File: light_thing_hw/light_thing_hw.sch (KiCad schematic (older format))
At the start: 63 parts, among them J1 CONNECTORS, J2 Li-Ion Battery, J3 ADDR_LED_PANEL_1_CONNECTORS, J4 ADDR_LED_PANEL_2_CONNECTORS, J5 MIC_CONN, J6 3V3_TP, Q1 MMBF170, Q2 BSS83P, SW1 ST_USER_BUTTON1, SW2 ST_RESET_BUTTON, U1 BC832-V1, U3 MCP73833T-FCI_UN, U4 LMR62421XMF, U5 LP38511MRX-ADJ_NOPB, U6 STM32L476RGTx, U7 ICM-20600

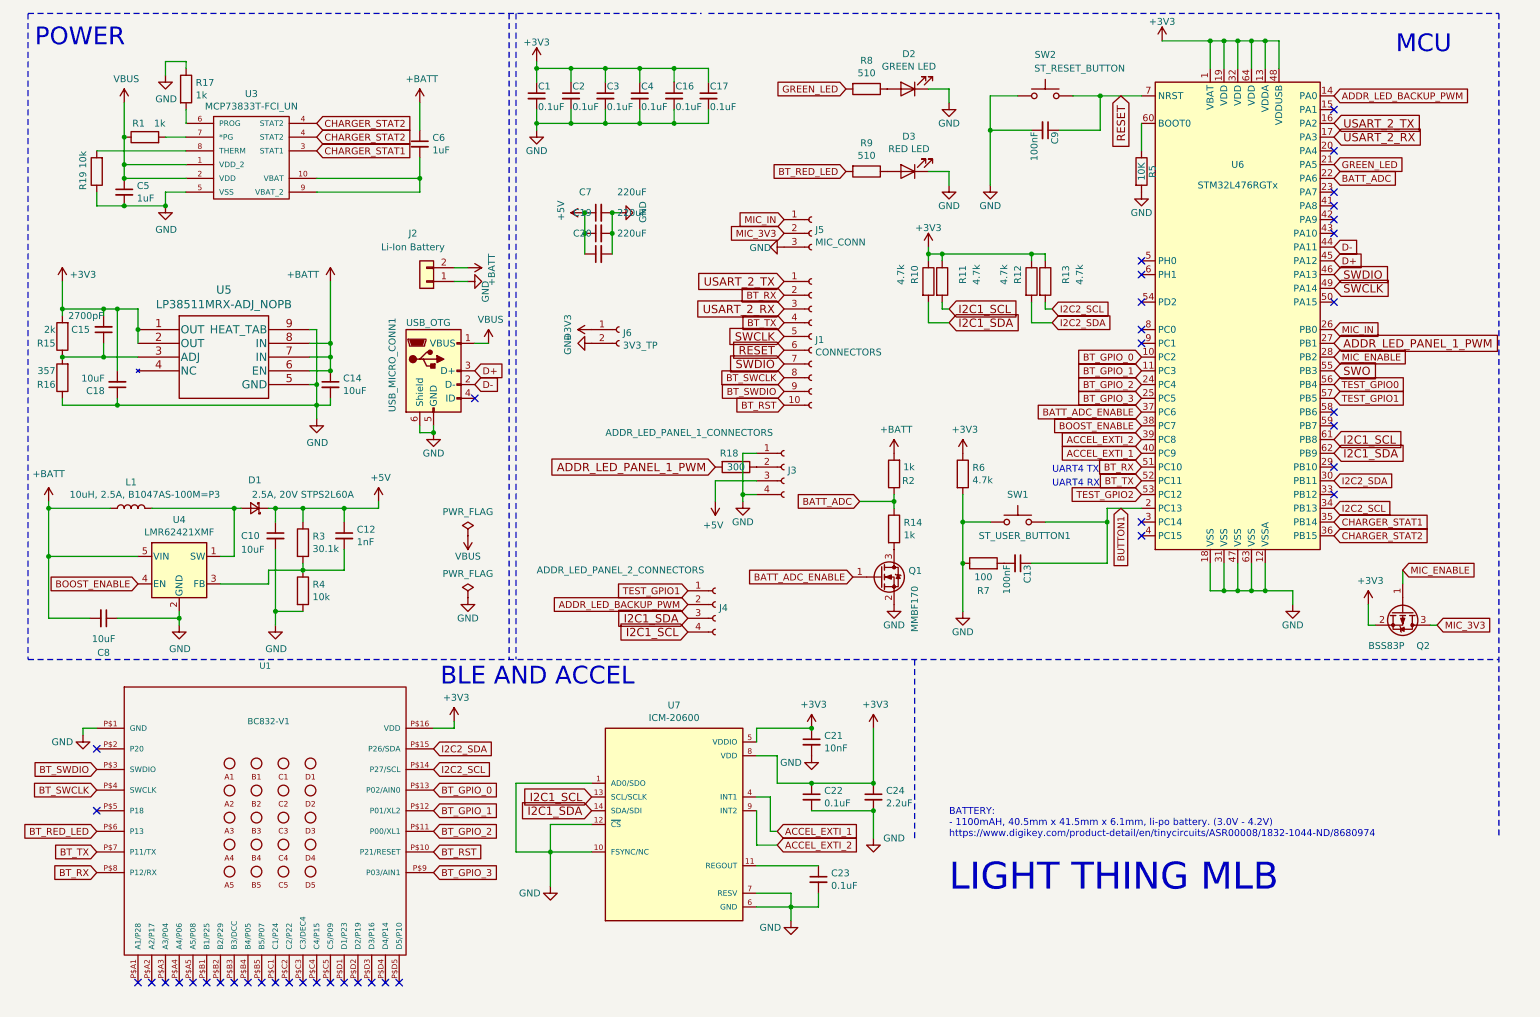
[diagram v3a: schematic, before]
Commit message: changed charger, reset button footprint
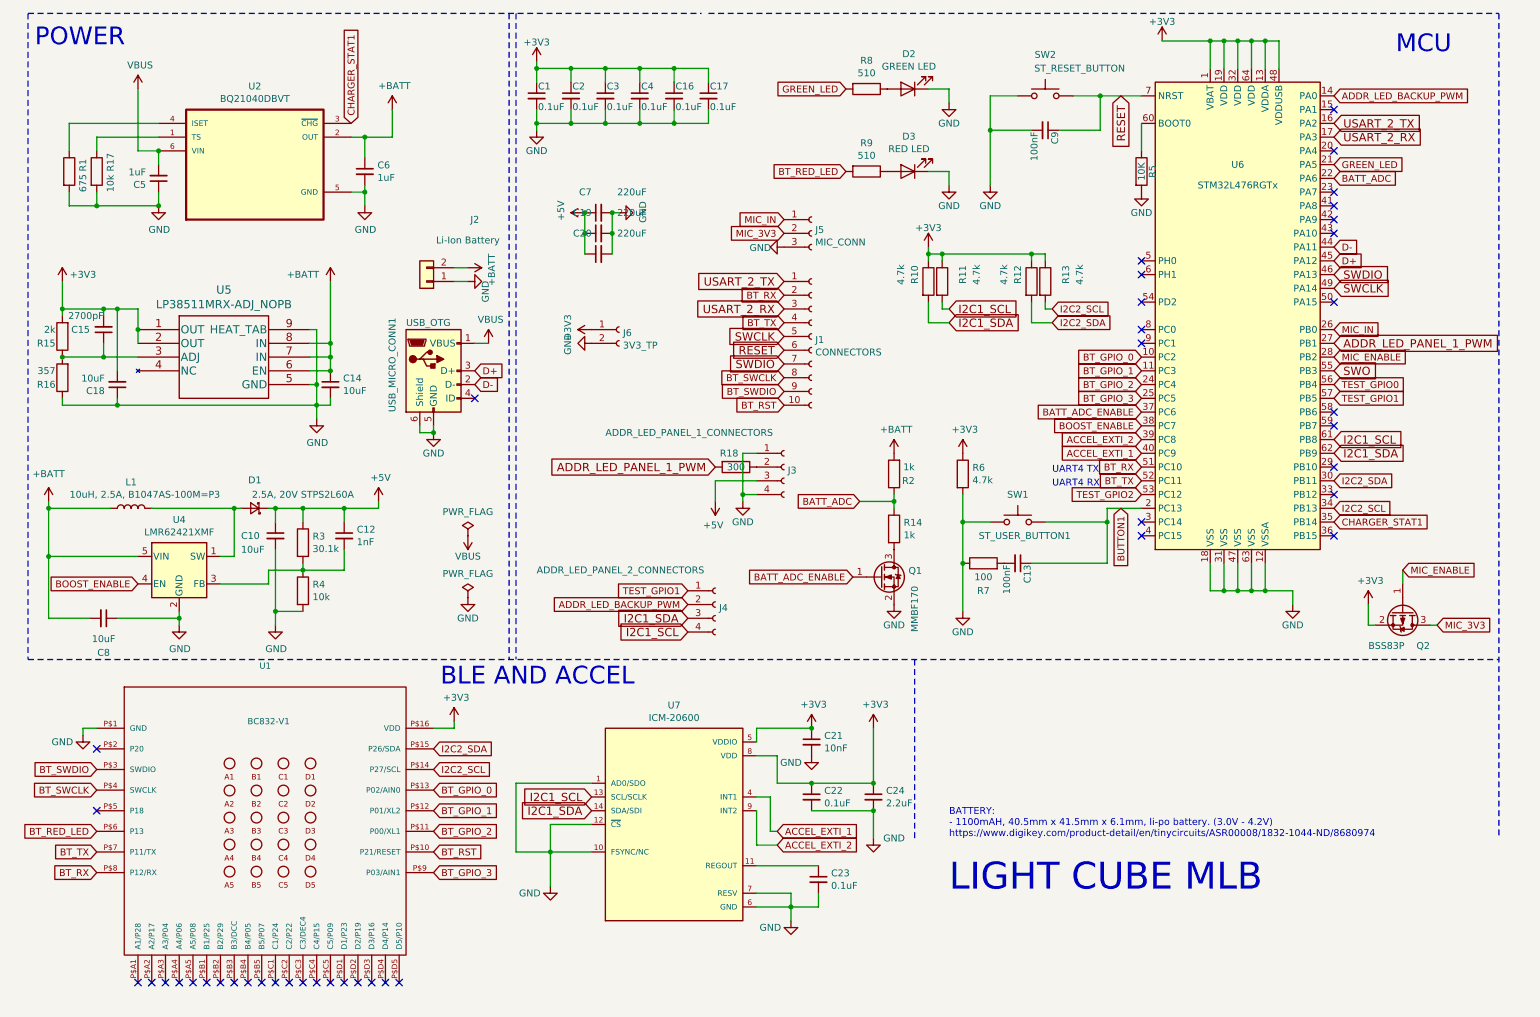
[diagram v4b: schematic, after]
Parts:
- removed R19: 10k, Resistor_SMD:R_0603_1608Metric_Pad1.05x0.95mm_HandSolder, symbol Device:R
- removed U3: MCP73833T-FCI_UN, footprints:MCP73833T-FCIUN-SMD, symbol MCP73833T-FCI_UN:MCP73833T-FCI_UN
- added U2: BQ21040DBVT, TI_BQ21040DBVT:SOT95P280X145-6N, symbol BQ21040DBVT:BQ21040DBVT
- R1: value 1k -> 675
- R17: value 1k -> 10k
- SW2: footprint Button_Switch_SMD:SW_SPST_PTS645 -> FSMSMTR_tactile_switch:SW_1437566-4
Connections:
- net +BATT: now also U2.2 (OUT)
- net CHARGER_STAT1: now also U2.3 (~CHG)
- net GND: now also C5.1, C6.2, R1.2, R17.2, U2.5 (GND); no longer C5.2, R17.1
- net VBUS: now also C5.2, U2.6 (VIN); no longer C5.1, R1.1
- net CHARGER_STAT2: no longer names the net of U6.36 (PB15)
- new net: R17.1, U2.1 (TS)
- new net: R1.1, U2.4 (ISET)
- no-connect marks 41 -> 42
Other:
- note added: "LIGHT CUBE MLB"
- note removed: "LIGHT THING MLB"
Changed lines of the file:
@@
 	11200 500  11200 6500
 Text Notes 7200 6900 0    196  ~ 0
-LIGHT THING MLB
+LIGHT CUBE MLB
 Connection ~ 8300 1100
 $Comp
@@
 U 1 1 5EC6ADFF
 P 3400 2450
-F 0 "J2" H 3500 2100 50  0000 C CNN
-F 1 "Li-Ion Battery" H 3500 2200 50  0000 C CNN
+F 0 "J2" H 3050 2000 50  0000 C CNN
+F 1 "Li-Ion Battery" H 3100 2150 50  0000 C CNN
 F 2 "Connector_JST:JST_SH_BM02B-SRSS-TB_1x02-1MP_P1.00mm_Vertical" H 3400 2450 50  0001 C CNN
 F 3 "~" H 3400 2450 50  0001 C CNN
@@
 F 0 "SW2" H 7900 1400 50  0000 C CNN
 F 1 "ST_RESET_BUTTON" H 8150 1300 50  0000 C CNN
-F 2 "Button_Switch_SMD:SW_SPST_PTS645" H 7900 1300 50  0001 C CNN
+F 2 "FSMSMTR_tactile_switch:SW_1437566-4" H 7900 1300 50  0001 C CNN
 F 3 "" H 7900 1300 50  0001 C CNN
 	1    7900 1100
@@
 BOOST_ENABLE
 $Comp
-L MCP73833T-FCI_UN:MCP73833T-FCI_UN U3
-U 1 1 5EF57FB2
-P 2450 1400
-F 0 "U3" H 2125 1715 50  0000 C CNN
-F 1 "MCP73833T-FCI_UN" H 2125 1624 50  0000 C CNN
-F 2 "footprints:MCP73833T-FCIUN-SMD" H 2500 1600 50  0001 L BNN
-F 3 "MSOP10" H 2900 1400 50  0001 L BNN
-F 4 "Microchip" H 2850 1500 50  0001 L BNN "Field4"
-F 5 "1605576" H 2900 1400 50  0001 L BNN "Field5"
-F 6 "88K5666" H 2900 1400 50  0001 L BNN "Field6"
-F 7 "MCP73833T-FCI/UN" H 2550 1700 50  0001 L BNN "Field7"
-	1    2450 1400
-	1    0    0    -1
-$EndComp
-$Comp
-L power:GND #PWR0104
-U 1 1 5EE8D240
-P 1500 1900
-F 0 "#PWR0104" H 1500 1650 50  0001 C CNN
-F 1 "GND" H 1505 1727 50  0000 C CNN
-F 2 "" H 1500 1900 50  0001 C CNN
-F 3 "" H 1500 1900 50  0001 C CNN
-	1    1500 1900
-	1    0    0    -1
-$EndComp
-Wire Wire Line
-	1500 1800 1500 1900
-Wire Wire Line
-	1650 1800 1500 1800
-$Comp
-L Device:R R1
-U 1 1 5EEA3D31
-P 1350 1400
-F 0 "R1" V 1450 1400 50  0000 L CNN
-F 1 "1k" V 1450 1250 50  0000 L CNN
-F 2 "Resistor_SMD:R_0603_1608Metric_Pad1.05x0.95mm_HandSolder" V 1280 1400 50  0001 C CNN
-F 3 "~" H 1350 1400 50  0001 C CNN
-F 4 "C21190" H 1350 1400 50  0001 C CNN "JLC_LIBRARY"
-	1    1350 1400
-	0    -1   -1   0
-$EndComp
-$Comp
-L Device:C_Small C5
-U 1 1 5EEAF533
-P 1200 1800
-F 0 "C5" H 1292 1846 50  0000 L CNN
-F 1 "1uF" H 1292 1755 50  0000 L CNN
-F 2 "Capacitor_SMD:C_0603_1608Metric_Pad1.05x0.95mm_HandSolder" H 1200 1800 50  0001 C CNN
-F 3 "~" H 1200 1800 50  0001 C CNN
-	1    1200 1800
-	1    0    0    -1
-$EndComp
-Wire Wire Line
-	1650 1700 1200 1700
-Wire Wire Line
-	1200 1700 1200 1600
-Wire Wire Line
-	1650 1600 1200 1600
-Connection ~ 1200 1600
-$Comp
 L power:VBUS #PWR0105
 U 1 1 5EEE9945
-P 1200 1150
-F 0 "#PWR0105" H 1200 1000 50  0001 C CNN
-F 1 "VBUS" H 1215 1323 50  0000 C CNN
-F 2 "" H 1200 1150 50  0001 C CNN
-F 3 "" H 1200 1150 50  0001 C CNN
-	1    1200 1150
-	1    0    0    -1
-$EndComp
-Connection ~ 1200 1700
-Wire Wire Line
-	1200 1900 1500 1900
-Connection ~ 1500 1900
-Wire Wire Line
-	1200 1150 1200 1400
-Connection ~ 1200 1400
-Wire Wire Line
-	1200 1400 1200 1600
-Wire Wire Line
-	1650 1400 1500 1400
-$Comp
-L Device:R R17
-U 1 1 5EF88860
-P 1650 1050
-F 0 "R17" H 1720 1096 50  0000 L CNN
-F 1 "1k" H 1720 1005 50  0000 L CNN
-F 2 "Resistor_SMD:R_0603_1608Metric_Pad1.05x0.95mm_HandSolder" V 1580 1050 50  0001 C CNN
-F 3 "~" H 1650 1050 50  0001 C CNN
-F 4 "C21190" H 1650 1050 50  0001 C CNN "JLC_LIBRARY"
-	1    1650 1050
-	1    0    0    -1
-$EndComp
-Wire Wire Line
-	3350 1800 3350 1700
-$Comp
-L Device:C_Small C6
-U 1 1 5EFBB5E4
-P 3350 1450
-F 0 "C6" H 3442 1496 50  0000 L CNN
-F 1 "1uF" H 3442 1405 50  0000 L CNN
-F 2 "Capacitor_SMD:C_0603_1608Metric_Pad1.05x0.95mm_HandSolder" H 3350 1450 50  0001 C CNN
-F 3 "~" H 3350 1450 50  0001 C CNN
-	1    3350 1450
-	1    0    0    -1
-$EndComp
-Wire Wire Line
-	3350 1700 3350 1550
-Connection ~ 3350 1700
-Wire Wire Line
-	3350 1350 3350 1150
+P 1300 1050
+F 0 "#PWR0105" H 1300 900 50  0001 C CNN
+F 1 "VBUS" H 1315 1223 50  0000 C CNN
+F 2 "" H 1300 1050 50  0001 C CNN
+F 3 "" H 1300 1050 50  0001 C CNN
+	1    1300 1050
+	1    0    0    -1
+$EndComp
+Wire Wire Line
+	3150 1400 3150 1200
 $Comp
 L power:+BATT #PWR0106
 U 1 1 5EFE21D4
-P 3350 1150
-F 0 "#PWR0106" H 3350 1000 50  0001 C CNN
-F 1 "+BATT" H 3365 1323 50  0000 C CNN
-F 2 "" H 3350 1150 50  0001 C CNN
-F 3 "" H 3350 1150 50  0001 C CNN
-	1    3350 1150
-	1    0    0    -1
-$EndComp
-$Comp
-L power:GND #PWR0107
-U 1 1 5F03E671
-P 1500 950
-F 0 "#PWR0107" H 1500 700 50  0001 C CNN
-F 1 "GND" H 1505 777 50  0000 C CNN
-F 2 "" H 1500 950 50  0001 C CNN
-F 3 "" H 1500 950 50  0001 C CNN
-	1    1500 950
-	1    0    0    -1
-$EndComp
-Wire Wire Line
-	1650 1200 1650 1300
-Wire Wire Line
-	1650 900  1650 850
-Wire Wire Line
-	1650 850  1500 850
-Wire Wire Line
-	1500 850  1500 950
+P 3150 1200
+F 0 "#PWR0106" H 3150 1050 50  0001 C CNN
+F 1 "+BATT" H 3165 1373 50  0000 C CNN
+F 2 "" H 3150 1200 50  0001 C CNN
+F 3 "" H 3150 1200 50  0001 C CNN
+	1    3150 1200
+	1    0    0    -1
+$EndComp
 Wire Wire Line
 	3750 2900 3850 2900
-Text GLabel 2600 1500 2    50   Input ~ 0
+Text GLabel 2850 1300 1    50   Input ~ 0
 CHARGER_STAT1
 Connection ~ 2700 3100
@@
 	3050 4100 2800 4100
 Connection ~ 2800 4100
-Wire Wire Line
-	2600 1800 3350 1800
-Wire Wire Line
-	2600 1700 3350 1700
 Text GLabel 5300 4800 0    50   Input ~ 0
 ADDR_LED_BACKUP_PWM
@@
 Text GLabel 10000 4200 2    50   Input ~ 0
 CHARGER_STAT1
-Text GLabel 10000 4300 2    50   Input ~ 0
-CHARGER_STAT2
 Text GLabel 10000 3000 2    50   Input ~ 0
 MIC_ENABLE
@@
 NoConn ~ 10000 3400
 NoConn ~ 10000 3500
-Wire Wire Line
-	1650 1500 1000 1500
-$Comp
-L Device:R R19
-U 1 1 6006B026
-P 1000 1650
-F 0 "R19" V 1100 1650 50  0000 L CNN
-F 1 "10k" V 1100 1500 50  0000 L CNN
-F 2 "Resistor_SMD:R_0603_1608Metric_Pad1.05x0.95mm_HandSolder" V 930 1650 50  0001 C CNN
-F 3 "~" H 1000 1650 50  0001 C CNN
-F 4 "C21190" H 1000 1650 50  0001 C CNN "JLC_LIBRARY"
-	1    1000 1650
-	-1   0    0    1
-$EndComp
-Wire Wire Line
-	1000 1800 1000 1900
-Wire Wire Line
-	1000 1900 1200 1900
-Connection ~ 1200 1900
 $Comp
 L power:GND #PWR0112
@@
 Text GLabel 5300 5000 0    60   Input ~ 0
 I2C1_SCL
-Text GLabel 2600 1400 2    50   Input ~ 0
-CHARGER_STAT2
-Text GLabel 2600 1300 2    50   Input ~ 0
-CHARGER_STAT2
 Text GLabel 6000 2100 0    50   Input ~ 0
 MIC_3V3
@@
 Wire Wire Line
 	4050 6600 4300 6600
+$Comp
+L BQ21040DBVT:BQ21040DBVT U2
+U 1 1 60135CA1
+P 2150 1600
+F 0 "U2" H 2150 2170 50  0000 C CNN
+F 1 "BQ21040DBVT" H 2150 2079 50  0000 C CNN
+F 2 "TI_BQ21040DBVT:SOT95P280X145-6N" H 2150 1600 50  0001 L BNN
+F 3 "" H 2150 1600 50  0001 L BNN
+	1    2150 1600
+	1    0    0    -1
+$EndComp
+Wire Wire Line
+	2850 1800 2950 1800
+Wire Wire Line
+	2950 1800 2950 1900
+$Comp
+L power:GND #PWR0104
+U 1 1 601452F4
+P 2950 1900
+F 0 "#PWR0104" H 2950 1650 50  0001 C CNN
+F 1 "GND" H 2955 1727 50  0000 C CNN
+F 2 "" H 2950 1900 50  0001 C CNN
+F 3 "" H 2950 1900 50  0001 C CNN
+	1    2950 1900
+	1    0    0    -1
+$EndComp
+Wire Wire Line
+	2950 1750 2950 1800
+Connection ~ 2950 1800
+Wire Wire Line
+	2950 1550 2950 1400
+Wire Wire Line
+	2950 1400 2850 1400
+Wire Wire Line
+	2950 1400 3150 1400
+Connection ~ 2950 1400
+$Comp
+L Device:R R17
+U 1 1 601ECAC0
+P 1000 1650
+F 0 "R17" V 1100 1650 50  0000 L CNN
+F 1 "10k" V 1100 1500 50  0000 L CNN
+F 2 "Resistor_SMD:R_0603_1608Metric_Pad1.05x0.95mm_HandSolder" V 930 1650 50  0001 C CNN
+F 3 "~" H 1000 1650 50  0001 C CNN
+F 4 "C21190" H 1000 1650 50  0001 C CNN "JLC_LIBRARY"
+	1    1000 1650
+	1    0    0    -1
+$EndComp
+$Comp
+L power:GND #PWR0107
+U 1 1 602388CD
+P 1450 1900
+F 0 "#PWR0107" H 1450 1650 50  0001 C CNN
+F 1 "GND" H 1455 1727 50  0000 C CNN
+F 2 "" H 1450 1900 50  0001 C CNN
+F 3 "" H 1450 1900 50  0001 C CNN
+	1    1450 1900
+	1    0    0    -1
+$EndComp
+Wire Wire Line
+	1000 1500 1000 1400
+Wire Wire Line
+	1000 1400 1450 1400
+Wire Wire Line
+	1000 1800 1000 1900
+Wire Wire Line
+	1000 1900 1450 1900
+$Comp
+L Device:R R1
+U 1 1 602AD118
+P 800 1650
+F 0 "R1" V 900 1650 50  0000 L CNN
+F 1 "675" V 900 1500 50  0000 L CNN
+F 2 "Resistor_SMD:R_0603_1608Metric_Pad1.05x0.95mm_HandSolder" V 730 1650 50  0001 C CNN
+F 3 "~" H 800 1650 50  0001 C CNN
+F 4 "C21190" H 800 1650 50  0001 C CNN "JLC_LIBRARY"
+	1    800  1650
+	1    0    0    -1
+$EndComp
+Wire Wire Line
+	1450 1300 800  1300
+Wire Wire Line
+	800  1300 800  1500
+Wire Wire Line
+	800  1800 800  1900
+Wire Wire Line
+	800  1900 1000 1900
+Connection ~ 1000 1900
+Wire Wire Line
+	1450 1500 1300 1500
+Wire Wire Line
+	1300 1500 1300 1050
+$Comp
+L Device:C_Small C5
+U 1 1 6022343E
+P 1450 1700
+F 0 "C5" H 1542 1746 50  0000 L CNN
+F 1 "1uF" H 1542 1655 50  0000 L CNN
+F 2 "Capacitor_SMD:C_0603_1608Metric_Pad1.05x0.95mm_HandSolder" H 1450 1700 50  0001 C CNN
+F 3 "~" H 1450 1700 50  0001 C CNN
+	1    1450 1700
+	-1   0    0    1
+$EndComp
+Wire Wire Line
+	1450 1600 1450 1500
+Connection ~ 1450 1500
+Wire Wire Line
+	1450 1800 1450 1900
+Connection ~ 1450 1900
+$Comp
+L Device:C_Small C6
+U 1 1 60153B88
+P 2950 1650
+F 0 "C6" H 3042 1696 50  0000 L CNN
+F 1 "1uF" H 3042 1605 50  0000 L CNN
+F 2 "Capacitor_SMD:C_0603_1608Metric_Pad1.05x0.95mm_HandSolder" H 2950 1650 50  0001 C CNN
+F 3 "~" H 2950 1650 50  0001 C CNN
+	1    2950 1650
+	1    0    0    -1
+$EndComp
+NoConn ~ 10000 4300
 $EndSCHEMATC
